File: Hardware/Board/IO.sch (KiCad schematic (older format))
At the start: 34 parts

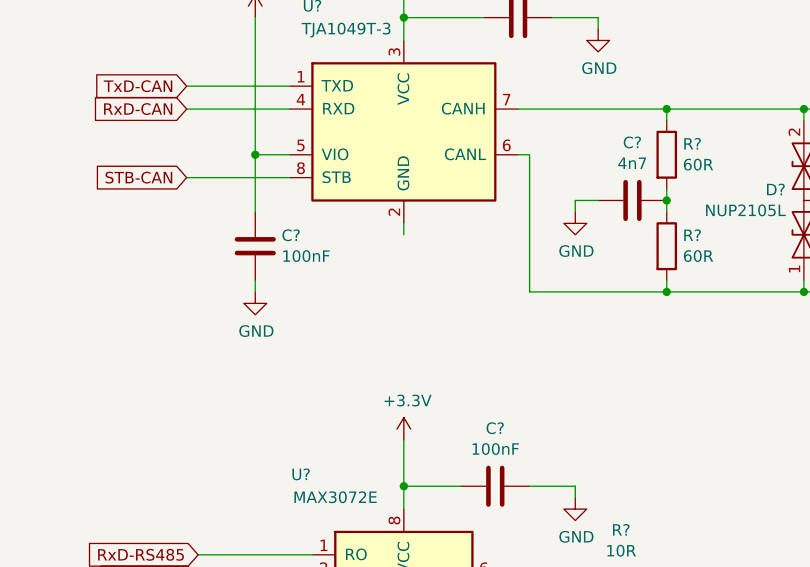
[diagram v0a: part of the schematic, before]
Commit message: Schaltregler Design fertig gestellt, Datenblätter hinzu gefügt.
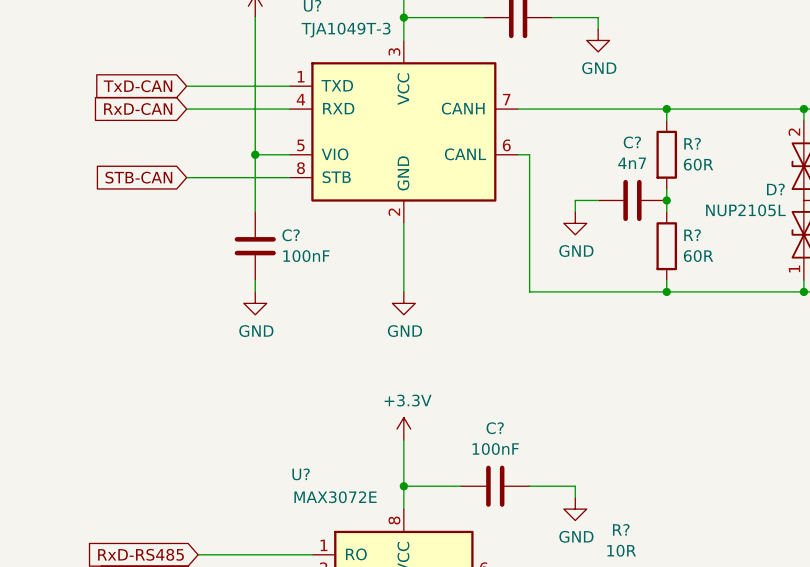
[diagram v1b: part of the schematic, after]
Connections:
- net GND: now also U?.2 (GND)
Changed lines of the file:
@@
 Wire Wire Line
 	5700 2700 5700 2750
-Wire Wire Line
-	6350 2450 6350 2500
 Text GLabel 5400 2250 0    50   Input ~ 0
 STB-CAN
@@
 Wire Wire Line
 	3850 2650 3850 2550
+$Comp
+L power:GND #PWR?
+U 1 1 5CBFA14C
+P 6350 2750
+F 0 "#PWR?" H 6350 2500 50  0001 C CNN
+F 1 "GND" H 6355 2577 50  0000 C CNN
+F 2 "" H 6350 2750 50  0001 C CNN
+F 3 "" H 6350 2750 50  0001 C CNN
+	1    6350 2750
+	1    0    0    -1
+$EndComp
+Wire Wire Line
+	6350 2450 6350 2750
 $EndSCHEMATC

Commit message: Netzliste und Board erstellt, hier sind noch Fehler im Bereich Footprints, BLE Modul nRF8001 hinzugefügt, erste Anschlussklemmen zugefügt
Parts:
- added FB1, FB2, FB3, FB4, FB5, FB6, FB7: 100R, Inductor_SMD:L_0603_1608Metric, symbol Device:Ferrite_Bead_Small
- C16, C17, C18, C19, C20, C21, C22, C23, C24, C25: renamed from C?; footprint (none) -> Capacitor_SMD:C_0603_1608Metric
- D10, D11: renamed from D?; footprint (none) -> Package_TO_SOT_SMD:SOT-23
- D4, D5, D6, D7, D8, D9: renamed from D?; footprint (none) -> Diode_SMD:D_SOD-323
- R1, R10, R11, R2, R3, R4, R5, R6, R7, R8, R9: renamed from R?; footprint (none) -> Resistor_SMD:R_0603_1608Metric
- gave numbers to parts that had none: 5
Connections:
- net CAN-H: now also FB4.1; no longer D10.2 (A2), R9.1, U6.7 (CANH)
- net CAN-L: now also FB5.1; no longer D10.1 (A1), R10.2, U6.6 (CANL)
- net LIN1: now also FB2.1; no longer C19.1, D8.1 (A1), R4.2, U3.6 (LIN)
- net LIN2: now also FB3.1; no longer C20.1, D9.1 (A1), R5.2, U4.6 (LIN)
- net LIN3: now also FB1.1; no longer C21.1, D7.1 (A1), R6.2, U5.6 (LIN)
- net RS485-A: now also FB6.1; no longer D11.2 (A2), R11.1, R7.1
- net RS485-B: now also FB7.1; no longer D11.1 (A1), R11.2, R8.1
- new net: C19.1, D8.1 (A1), FB2.2, R4.2, U3.6 (LIN)
- new net: C20.1, D9.1 (A1), FB3.2, R5.2, U4.6 (LIN)
- new net: C21.1, D7.1 (A1), FB1.2, R6.2, U5.6 (LIN)
- new net: D10.1 (A1), FB5.2, R10.2, U6.6 (CANL)
- new net: D10.2 (A2), FB4.2, R9.1, U6.7 (CANH)
- new net: D11.2 (A2), FB6.2, R11.1, R7.1
- new net: D11.1 (A1), FB7.2, R11.2, R8.1

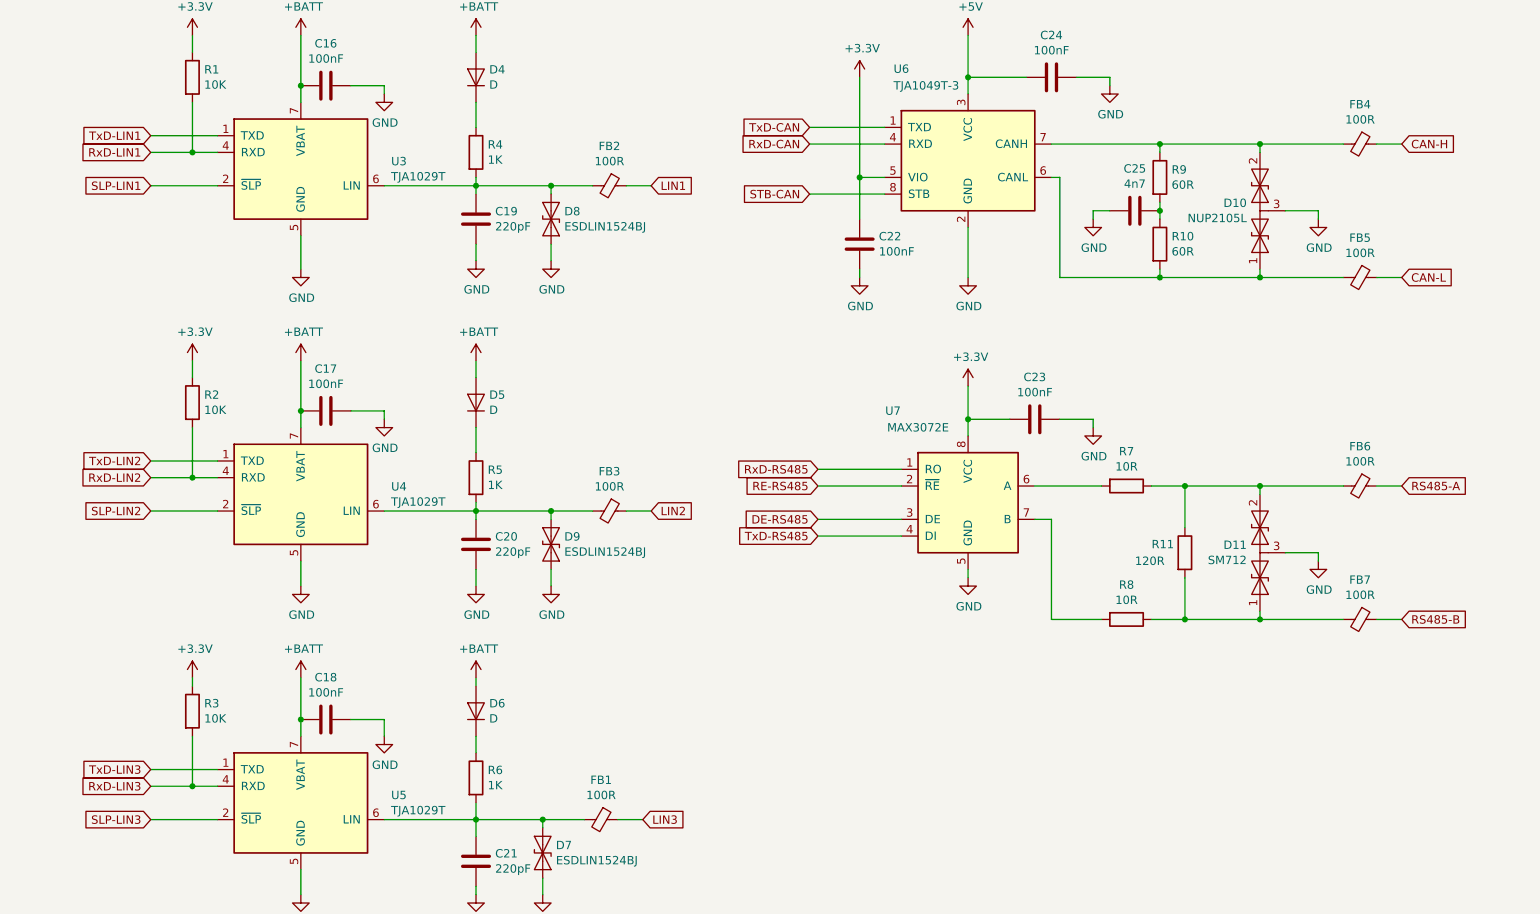
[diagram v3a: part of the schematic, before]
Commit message: Port Bezeichnungen am Prozessor korrigiert, Schnittstellen angepasst.
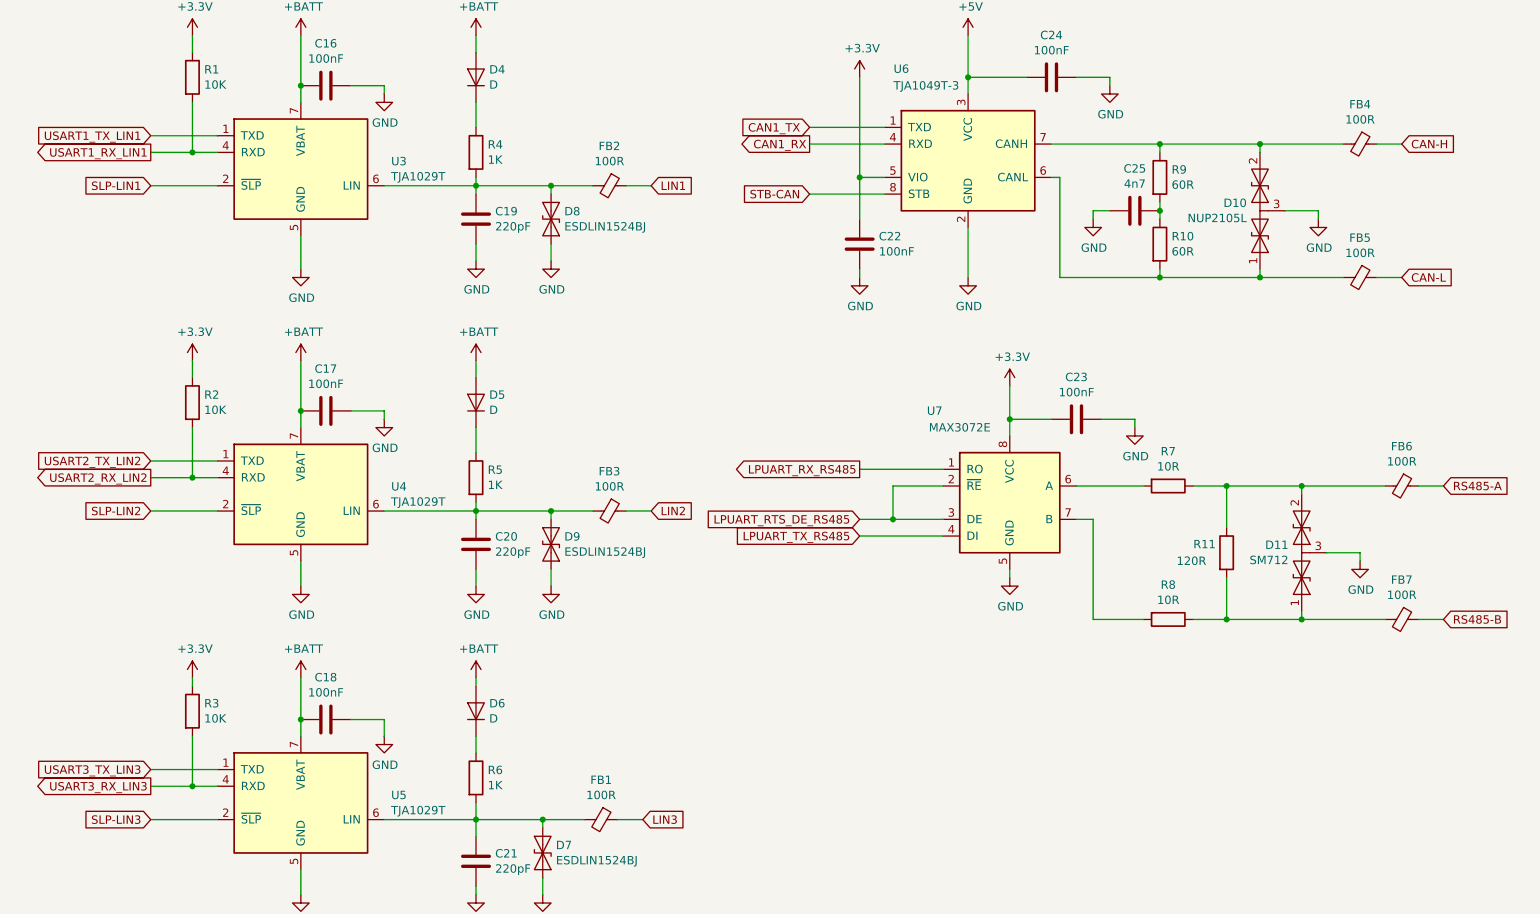
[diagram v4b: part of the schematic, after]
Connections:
- net RE-RS485 is gone; now on net LPUART_RTS_DE_RS485: U7.2 (~RE~)
- net DE-RS485 renamed LPUART_RTS_DE_RS485
- net RxD-CAN renamed CAN1_RX
- net RxD-LIN1 renamed USART1_RX_LIN1
- net RxD-LIN2 renamed USART2_RX_LIN2
- net RxD-LIN3 renamed USART3_RX_LIN3
- net RxD-RS485 renamed LPUART_RX_RS485
- net TxD-CAN renamed CAN1_TX
- net TxD-LIN1 renamed USART1_TX_LIN1
- net TxD-LIN2 renamed USART2_TX_LIN2
- net TxD-LIN3 renamed USART3_TX_LIN3
- net TxD-RS485 renamed LPUART_TX_RS485
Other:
- moved on the sheet: C23, D11, FB6, FB7, R11, R7, R8, U7

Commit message: Eine Menge Arbeit auf der GPN, fast fertig im Schaltplan.
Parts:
- added C?: 100nF, Capacitor_SMD:C_0603_1608Metric, symbol Device:C
- added R? (x2): 10K, Resistor_SMD:R_0603_1608Metric, symbol Device:R
- added U?: PCF8574A, symbol Interface_Expansion:PCF8574A
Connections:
- net +3V3: now also C?.2, R?.1, R?.1, U?.1 (A0), U?.16 (VDD)
- net GND: now also C?.1, U?.2 (A1), U?.3 (A2), U?.8 (VSS); no longer D7.2 (A2)
- net SLP-LIN1: now also U?.4 (P0)
- net SLP-LIN2: now also U?.5 (P1)
- net SLP-LIN3: now also U?.6 (P2)
- net STB-CAN: now also U?.7 (P3)
- net USART1_RX_LIN1: now also U3.1 (TXD); no longer U3.4 (RXD)
- net USART1_TX_LIN1: now also U3.4 (RXD); no longer U3.1 (TXD)
- net USART2_RX_LIN2: now also U4.1 (TXD); no longer U4.4 (RXD)
- net USART2_TX_LIN2: now also U4.4 (RXD); no longer U4.1 (TXD)
- net USART3_RX_LIN3: now also U5.1 (TXD); no longer U5.4 (RXD)
- net USART3_TX_LIN3: now also U5.4 (RXD); no longer U5.1 (TXD)
- new net 3VA_EN: U?.10 (P5)
- new net 5V_EN: U?.9 (P4)
- new net 5V_Raspi_EN: U?.11 (P6)
- new net I2C2_SCL: R?.2, U?.14 (SCL)
- new net I2C2_SDA: R?.2, U?.15 (SDA)
- new net VSW_Disp_EN: U?.12 (P7)
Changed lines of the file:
@@
 EESchema Schematic File Version 4
 LIBS:Womo-cache
-EELAYER 26 0
+EELAYER 29 0
 EELAYER END
-$Descr A4 11693 8268
+$Descr A3 16535 11693
 encoding utf-8
 Sheet 2 7
@@
 	1    0    0    -1
 $EndComp
-Text GLabel 1450 1900 0    50   Input ~ 0
+Text GLabel 1450 2000 0    50   Input ~ 0
 USART1_TX_LIN1
-Text GLabel 1450 2000 0    50   Output ~ 0
+Text GLabel 1450 1900 0    50   Output ~ 0
 USART1_RX_LIN1
-Text GLabel 1450 3850 0    50   Input ~ 0
+Text GLabel 1450 3950 0    50   Input ~ 0
 USART2_TX_LIN2
-Text GLabel 1450 3950 0    50   Output ~ 0
+Text GLabel 1450 3850 0    50   Output ~ 0
 USART2_RX_LIN2
-Text GLabel 1450 5700 0    50   Input ~ 0
+Text GLabel 1450 5800 0    50   Input ~ 0
 USART3_TX_LIN3
-Text GLabel 1450 5800 0    50   Output ~ 0
+Text GLabel 1450 5700 0    50   Output ~ 0
 USART3_RX_LIN3
 Text GLabel 5400 1850 0    50   Input ~ 0
@@
 $EndComp
 Wire Wire Line
-	1450 1900 1850 1900
-Wire Wire Line
-	1450 2000 1700 2000
-Wire Wire Line
-	1700 1700 1700 2000
-Connection ~ 1700 2000
-Wire Wire Line
-	1700 2000 1850 2000
-Wire Wire Line
-	1450 3850 1850 3850
-Wire Wire Line
-	1450 3950 1700 3950
-Wire Wire Line
-	1700 3650 1700 3950
-Connection ~ 1700 3950
-Wire Wire Line
-	1700 3950 1850 3950
-Wire Wire Line
-	1850 5700 1450 5700
-Wire Wire Line
-	1850 5800 1700 5800
-Wire Wire Line
-	1700 5500 1700 5800
-Connection ~ 1700 5800
-Wire Wire Line
-	1700 5800 1450 5800
+	1450 1900 1700 1900
+Wire Wire Line
+	1450 3850 1700 3850
+Wire Wire Line
+	1850 5700 1700 5700
 $Comp
 L power:+3.3V #PWR0105
@@
 L power:GND #PWR0153
 U 1 1 5CA67402
-P 3800 6450
-F 0 "#PWR0153" H 3800 6200 50  0001 C CNN
-F 1 "GND" H 3805 6277 50  0000 C CNN
-F 2 "" H 3800 6450 50  0001 C CNN
-F 3 "" H 3800 6450 50  0001 C CNN
-	1    3800 6450
+P 7200 7400
+F 0 "#PWR0153" H 7200 7150 50  0001 C CNN
+F 1 "GND" H 7205 7227 50  0000 C CNN
+F 2 "" H 7200 7400 50  0001 C CNN
+F 3 "" H 7200 7400 50  0001 C CNN
+	1    7200 7400
 	1    0    0    -1
 $EndComp
@@
 Wire Wire Line
 	5900 4200 6200 4200
+Wire Wire Line
+	1450 2000 1850 2000
+Wire Wire Line
+	1700 1700 1700 1900
+Connection ~ 1700 1900
+Wire Wire Line
+	1700 1900 1850 1900
+Wire Wire Line
+	1450 3950 1850 3950
+Wire Wire Line
+	1700 3650 1700 3850
+Connection ~ 1700 3850
+Wire Wire Line
+	1700 3850 1850 3850
+Wire Wire Line
+	1450 5800 1850 5800
+Wire Wire Line
+	1700 5500 1700 5700
+Connection ~ 1700 5700
+Wire Wire Line
+	1700 5700 1450 5700
+Text GLabel 5650 6300 0    50   BiDi ~ 0
+I2C2_SDA
+Text GLabel 5650 6200 0    50   Input ~ 0
+I2C2_SCL
+$Comp
+L Interface_Expansion:PCF8574A U?
+U 1 1 5CF888F7
+P 7200 6600
+F 0 "U?" H 6750 7350 50  0000 C CNN
+F 1 "PCF8574A" H 6850 7250 50  0000 C CNN
+F 2 "" H 7200 6600 50  0001 C CNN
+F 3 "http://www.nxp.com/documents/data_sheet/PCF8574_PCF8574A.pdf" H 7200 6600 50  0001 C CNN
+	1    7200 6600
+	1    0    0    -1
+$EndComp
+Text GLabel 7850 6200 2    50   Output ~ 0
+SLP-LIN1
+Text GLabel 7850 6300 2    50   Output ~ 0
+SLP-LIN2
+Text GLabel 7850 6400 2    50   Output ~ 0
+SLP-LIN3
+Text GLabel 7850 6500 2    50   Output ~ 0
+STB-CAN
+Wire Wire Line
+	7700 6500 7850 6500
+Wire Wire Line
+	7700 6400 7850 6400
+Wire Wire Line
+	7700 6300 7850 6300
+Wire Wire Line
+	7700 6200 7850 6200
+$Comp
+L power:GND #PWR?
+U 1 1 5CFC8198
+P 6350 6750
+F 0 "#PWR?" H 6350 6500 50  0001 C CNN
+F 1 "GND" H 6355 6577 50  0000 C CNN
+F 2 "" H 6350 6750 50  0001 C CNN
+F 3 "" H 6350 6750 50  0001 C CNN
+	1    6350 6750
+	1    0    0    -1
+$EndComp
+Wire Wire Line
+	6350 6600 6350 6700
+Connection ~ 6350 6700
+Wire Wire Line
+	6350 6700 6350 6750
+$Comp
+L power:+3.3V #PWR?
+U 1 1 5CFDD90C
+P 7200 5650
+F 0 "#PWR?" H 7200 5500 50  0001 C CNN
+F 1 "+3.3V" H 7215 5823 50  0000 C CNN
+F 2 "" H 7200 5650 50  0001 C CNN
+F 3 "" H 7200 5650 50  0001 C CNN
+	1    7200 5650
+	1    0    0    -1
+$EndComp
+$Comp
+L Device:C C?
+U 1 1 5CFE3BF0
+P 7450 5750
+F 0 "C?" V 7198 5750 50  0000 C CNN
+F 1 "100nF" V 7289 5750 50  0000 C CNN
+F 2 "Capacitor_SMD:C_0603_1608Metric" H 7488 5600 50  0001 C CNN
+F 3 "~" H 7450 5750 50  0001 C CNN
+	1    7450 5750
+	0    1    1    0
+$EndComp
+$Comp
+L power:GND #PWR?
+U 1 1 5CFE91D8
+P 7900 5800
+F 0 "#PWR?" H 7900 5550 50  0001 C CNN
+F 1 "GND" H 7905 5627 50  0000 C CNN
+F 2 "" H 7900 5800 50  0001 C CNN
+F 3 "" H 7900 5800 50  0001 C CNN
+	1    7900 5800
+	1    0    0    -1
+$EndComp
+Wire Wire Line
+	7200 5650 7200 5750
+Wire Wire Line
+	7300 5750 7200 5750
+Connection ~ 7200 5750
+Wire Wire Line
+	7200 5750 7200 5900
+Wire Wire Line
+	7900 5750 7900 5800
+Wire Wire Line
+	7600 5750 7900 5750
+$Comp
+L Device:R R?
+U 1 1 5D005AC4
+P 6150 5900
+F 0 "R?" H 6220 5946 50  0000 L CNN
+F 1 "10K" H 6220 5855 50  0000 L CNN
+F 2 "Resistor_SMD:R_0603_1608Metric" V 6080 5900 50  0001 C CNN
+F 3 "~" H 6150 5900 50  0001 C CNN
+	1    6150 5900
+	1    0    0    -1
+$EndComp
+$Comp
+L power:+3.3V #PWR?
+U 1 1 5D005ACA
+P 6150 5650
+F 0 "#PWR?" H 6150 5500 50  0001 C CNN
+F 1 "+3.3V" H 6165 5823 50  0000 C CNN
+F 2 "" H 6150 5650 50  0001 C CNN
+F 3 "" H 6150 5650 50  0001 C CNN
+	1    6150 5650
+	1    0    0    -1
+$EndComp
+Wire Wire Line
+	6150 5750 6150 5650
+$Comp
+L Device:R R?
+U 1 1 5D00C9F0
+P 5850 5900
+F 0 "R?" H 5920 5946 50  0000 L CNN
+F 1 "10K" H 5920 5855 50  0000 L CNN
+F 2 "Resistor_SMD:R_0603_1608Metric" V 5780 5900 50  0001 C CNN
+F 3 "~" H 5850 5900 50  0001 C CNN
+	1    5850 5900
+	1    0    0    -1
+$EndComp
+$Comp
+L power:+3.3V #PWR?
+U 1 1 5D00C9F6
+P 5850 5650
+F 0 "#PWR?" H 5850 5500 50  0001 C CNN
+F 1 "+3.3V" H 5865 5823 50  0000 C CNN
+F 2 "" H 5850 5650 50  0001 C CNN
+F 3 "" H 5850 5650 50  0001 C CNN
+	1    5850 5650
+	1    0    0    -1
+$EndComp
+Wire Wire Line
+	5850 5750 5850 5650
+Wire Wire Line
+	5650 6200 5850 6200
+Wire Wire Line
+	5650 6300 6150 6300
+Wire Wire Line
+	5850 6050 5850 6200
+Connection ~ 5850 6200
+Wire Wire Line
+	5850 6200 6700 6200
+Wire Wire Line
+	6150 6050 6150 6300
+Connection ~ 6150 6300
+Wire Wire Line
+	6150 6300 6700 6300
+Wire Wire Line
+	7200 7300 7200 7400
+Text GLabel 7850 6900 2    50   Output ~ 0
+VSW_Disp_EN
+Text GLabel 7850 6800 2    50   Output ~ 0
+5V_Raspi_EN
+Text GLabel 7850 6700 2    50   Output ~ 0
+3VA_EN
+Text GLabel 7850 6600 2    50   Output ~ 0
+5V_EN
+Wire Wire Line
+	7850 6600 7700 6600
+Wire Wire Line
+	7850 6700 7700 6700
+Wire Wire Line
+	7850 6800 7700 6800
+Wire Wire Line
+	7850 6900 7700 6900
+Wire Wire Line
+	6350 6600 6700 6600
+Wire Wire Line
+	6350 6700 6700 6700
+Wire Wire Line
+	6700 6500 6450 6500
+Wire Wire Line
+	6450 6500 6450 5750
+Wire Wire Line
+	6450 5750 7200 5750
 $EndSCHEMATC
